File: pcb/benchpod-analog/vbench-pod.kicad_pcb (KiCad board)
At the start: 4 copper layers, 98.5 x 120.2 mm, 236 parts, among them CN1 KH-FPC1.0-H2.0SMT-24P-QCHF, J10 BNC-KYWE-295-W4-N, J11 WJ15EDGRC-3.81-06P, J8 WJ15EDGRC-3.81-02P, J9 WJ15EDGRC-3.81-02P, K1 G6K-2F-Y DC5, K2 G6K-2F-Y DC5, K3 G6K-2F-Y DC5, K4 G6K-2F-Y DC5, Q1 BCP56, U15 TPS7A2045PDBVR, U16 TLV61046ADBVR, U17 TMCP1A106MTRF, U3 TPS7A2050PDQNR, U30 AP2112K-3.3, U36 MCP33131D-10-E/MS, U37 THS4551IRUNR, U38 ADR4540BRZ-R7, U39 AP2112K-1.8TRG1, U40 OPA810IDBVR, U41 LM27761DSGR, U42 LM7705MM/NOPB, U43 DAC8554IPWR, U44 OPA2365AIDR, U45 OPA2992IDR, U46 AP2112K-3.3, U49 TPS65131RGER, U50 TPS7A1901DRBR, U51 OPA2992IDR, U53 TPL7407LAPWR, U58 TCA9554PWR, U61 24C32, U9 XTR116UA/2K5

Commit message: analog: black DORABO terminals, flush with the front panel
J8/J9 -> DB2ERC-3.81-2P-BK (C5259145, same as digital J4-J6), J11 -> DB2ERC-3.81-6P-BK
(C5244107, new footprint from EasyEDA + courtyard, no 3D model). Same pinout and pitch,
body centre x kept, pad row y 25.53 -> 24.271 (face 3.8 mm past the edge). Stale
C8465/WJ500V fields on J8/J9 corrected. Tracks to the old pads need rerouting.

Co-Authored-By: Claude Opus 5.5 <noreply@anthropic.com>
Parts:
- J11: value WJ15EDGRC-3.81-06P -> DB2ERC-3.81-6P-BK; footprint lcsc_footprints:C7246_CONN-TH_WJ15EDGRC-3.81-6P -> lcsc_footprints:C5244107_HDR-TH_DB2ERC-3.81-6P-BK
- J8, J9: value WJ15EDGRC-3.81-02P -> DB2ERC-3.81-2P-BK; footprint lcsc_footprints:C8387_CONN-TH_2P-P3.81_WJ15EDGRC-3.81-2P -> lcsc_footprints:C5259145_CONN-TH_2P-P3.81_DB2ERC-3.81-2P-BK
- moved J11 1.26 mm to (115.2, 24.3)
- moved J8 1.26 mm to (74.6, 24.3)
- moved J9 1.26 mm to (91.1, 24.3)

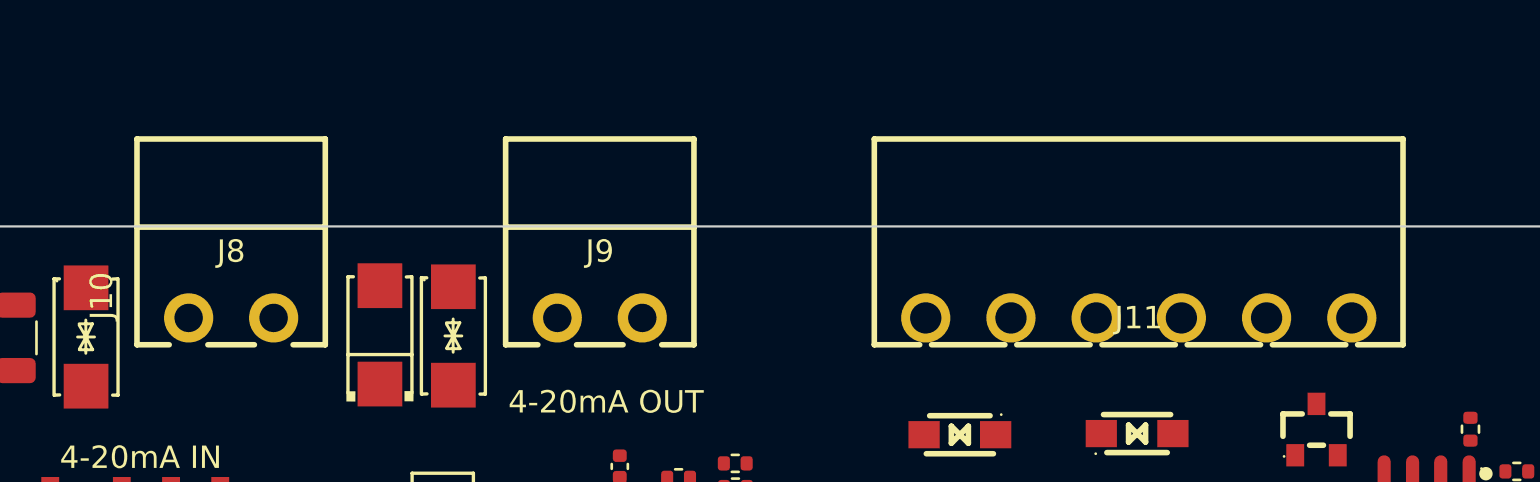
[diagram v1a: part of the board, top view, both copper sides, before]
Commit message: analog: J8/J9/J11 0.09 mm toward the front (face 0.1 mm behind panel outside, per enclosure fit check)
Co-Authored-By: Claude Opus 5.5 <noreply@anthropic.com>
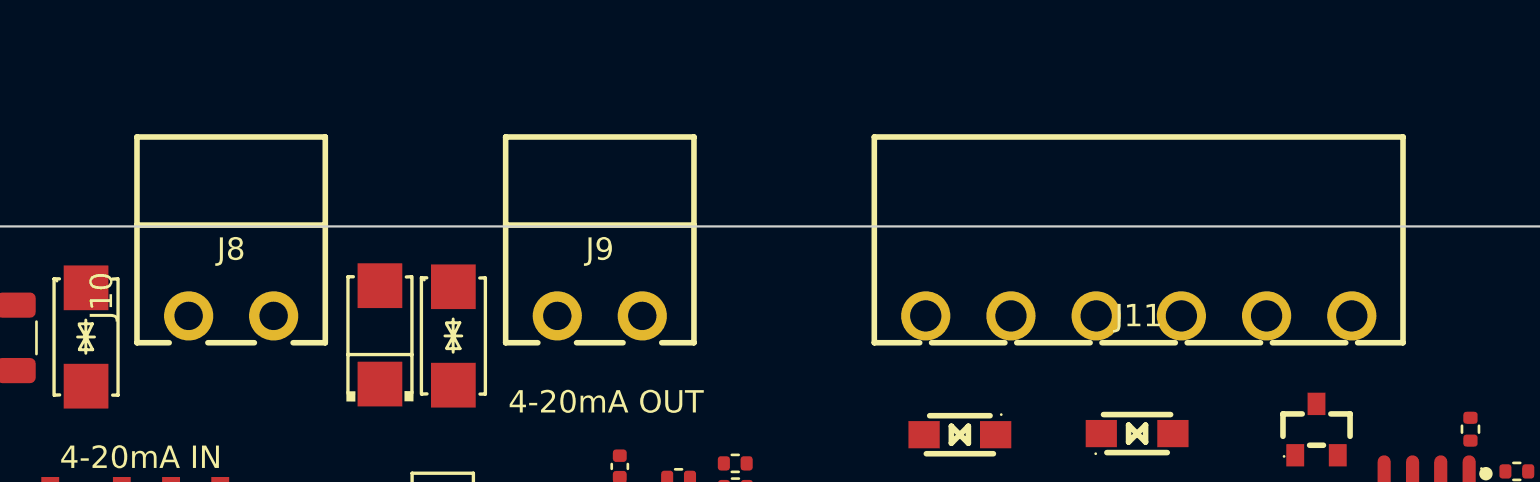
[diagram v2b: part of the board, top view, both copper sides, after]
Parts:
- moved J11 0.09 mm to (115.2, 24.2)
- moved J8 0.09 mm to (74.6, 24.2)
- moved J9 0.09 mm to (91.1, 24.2)
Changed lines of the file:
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@@
 	(footprint "lcsc_footprints:C5259145_CONN-TH_2P-P3.81_DB2ERC-3.81-2P-BK"
 		(layer "F.Cu")
-		(at 74.634 24.271 180)
+		(at 74.634 24.181 180)
 		(property "Reference" "J8"
 			(at 0 2.975 180)
@@
 	(footprint "lcsc_footprints:C5259145_CONN-TH_2P-P3.81_DB2ERC-3.81-2P-BK"
 		(layer "F.Cu")
-		(at 91.118 24.271 180)
+		(at 91.118 24.181 180)
 		(property "Reference" "J9"
 			(at 0 2.975 180)
@@
 	(footprint "lcsc_footprints:C5244107_HDR-TH_DB2ERC-3.81-6P-BK"
 		(layer "F.Cu")
-		(at 115.211999 24.271 180)
+		(at 115.211999 24.181 180)
 		(descr "DORABO DB2ERC-3.81-6P-BK, 6-pin 3.81 mm pluggable terminal, black (LCSC C5244107)")
 		(property "Reference" "J11"
